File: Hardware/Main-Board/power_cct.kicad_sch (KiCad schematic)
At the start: 43 parts, among them J7 Conn_01x02, Q10 AO3400A, Q5 MGSF1N02LT1G, Q7 IPD90P03P4L-04-HXY, Q8 CJ3401, Q9 AO3400A, SW1 TL3330AF260QG, U2 bq34210-Q1, U6 BQ25601, U7 TPS63000

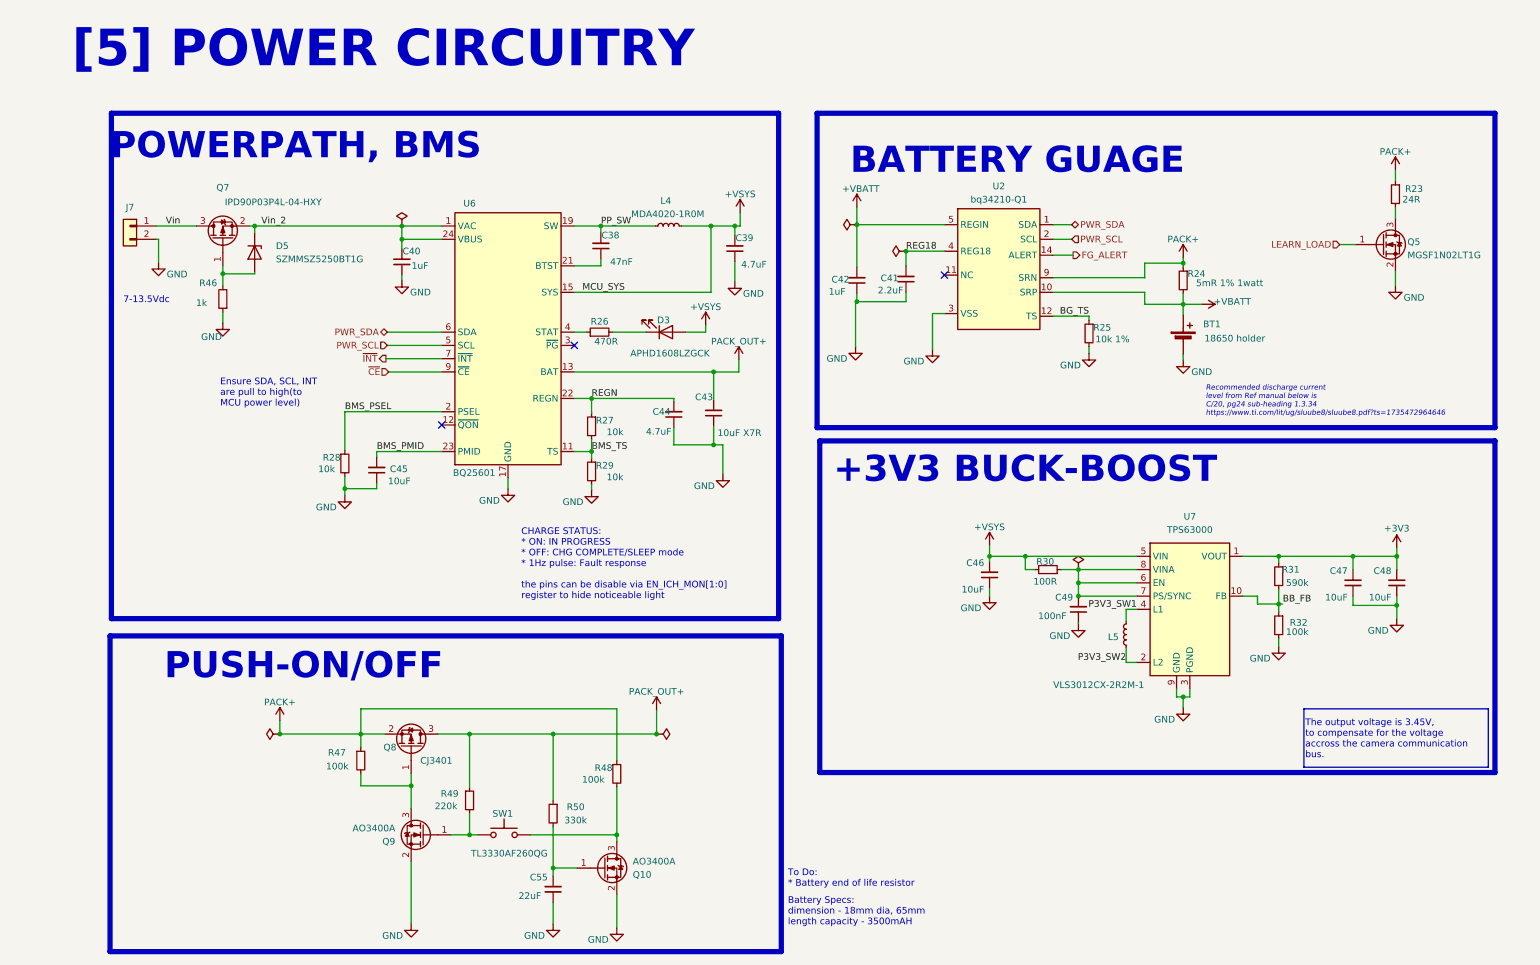
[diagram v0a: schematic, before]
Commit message: Done with main board design, and camera interconnect in progress
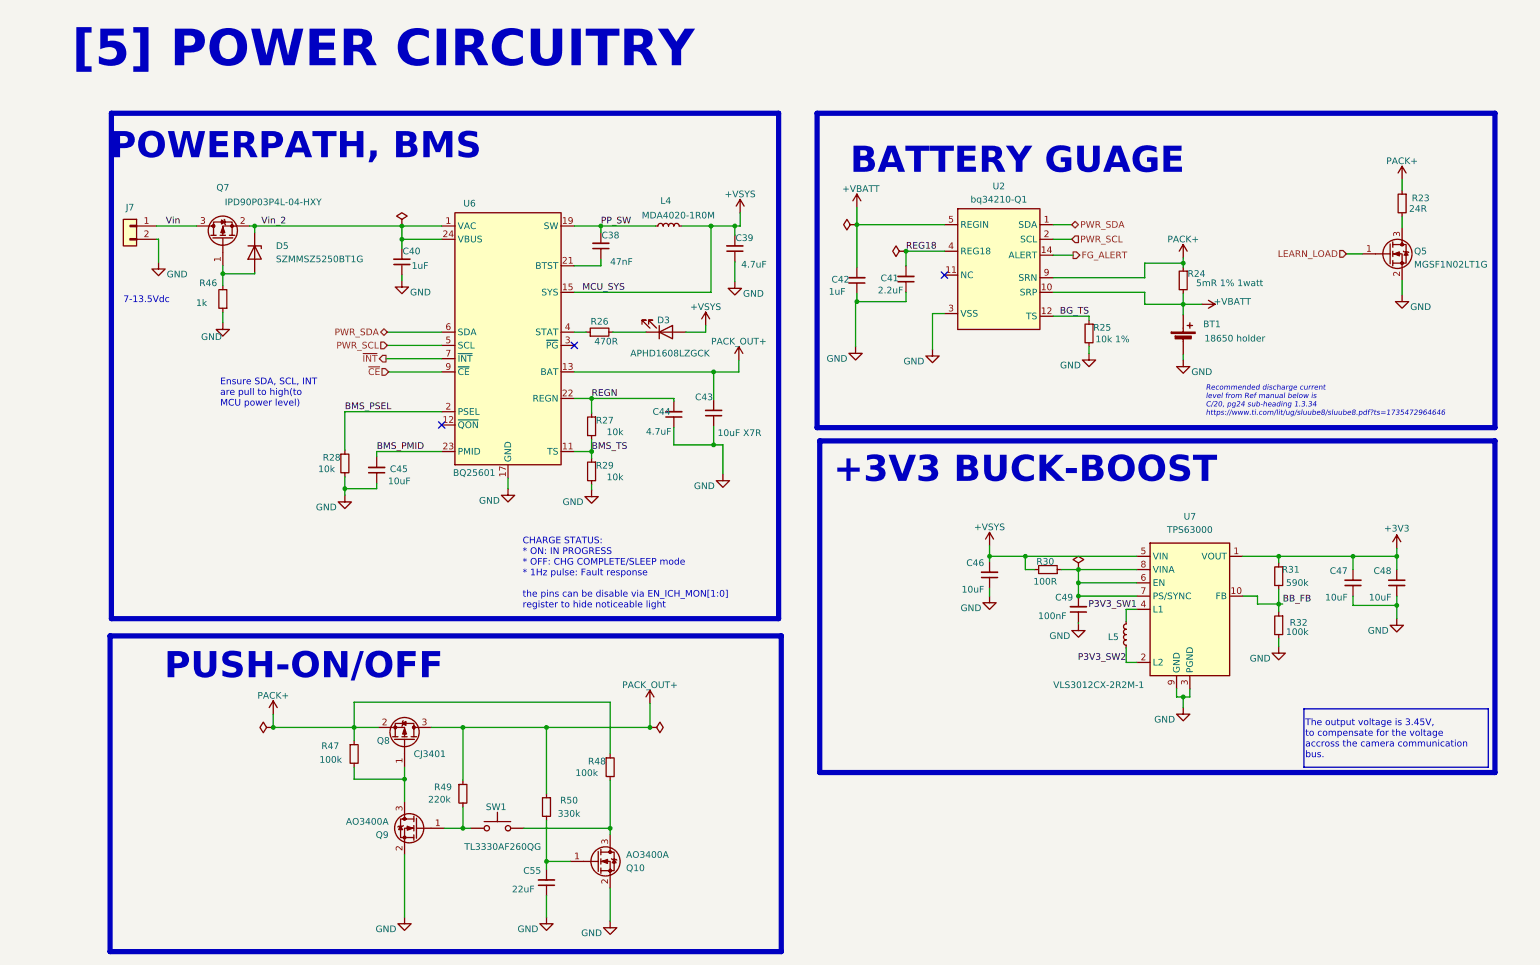
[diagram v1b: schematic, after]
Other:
- note removed: "Battery Specs: dimension - 18mm dia, 65mm length capacity - 3500mAH"
- note removed: "To Do: * Battery end of life resistor"
- moved on the sheet: C55, Q10, Q5, Q8, Q9, R23, R47, R48, R49, R50, SW1
